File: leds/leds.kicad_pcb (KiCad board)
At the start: 4 copper layers, 68.8 x 135.2 mm, 96 parts, among them CN1 39302030, CN2 39288020, CN3 39288020, CN4 39288020, CN5 39302030, CN6 39288020, CN7 39288020, CN701 BM04B-SRSS-TB(LF)(SN), CN8 39288020, J202 Conn_01x06, J301 Conn_01x05_Pin, Q701 BSS138, Q702 BSS138, SW201 KEY-SMD_B3U-1000PM, SW202 KEY-SMD_B3U-1000PM, U1 SN74AHCT125PWR, U2 BTS70021EPPXUMA1, U201 ESP32-S3-WROOM-1, U3 BTS70021EPPXUMA1, U301 TPD6S300A, U302 TPS25730D, U401 TPS54202DDC, U402 CYA1040-15UH, U701 TPS73733DCQ_C5220270

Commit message: first draft
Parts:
- removed the CN5 at (-20.1, 157.0)
- removed LED201, LED202, LED203, LED204, LED205, LED206, LED207, LED208, LED209: WS2812B-2020, easyeda2kicad:LED-SMD_4P-L2.0-W2.0-TL_WS2812B-2020
- removed the U2 at (-35.5, 168.2)
- added CN10: 39302030, easyeda2kicad:CONN-TH_3P-P4.20_39302030, F.Cu at (105.6, 110.1)
- added CN11: 39288020, easyeda2kicad:CONN-TH_39288020, F.Cu at (105.9, 120.0)
- added CN12: 39288020, easyeda2kicad:CONN-TH_39288020, F.Cu at (105.9, 128.5)
- added CN13: 39288020, easyeda2kicad:CONN-TH_39288020, F.Cu at (105.9, 136.5)
- added CN14: 39302030, easyeda2kicad:CONN-TH_3P-P4.20_39302030, F.Cu at (140.6, 110.1)
- added CN15: 39288020, easyeda2kicad:CONN-TH_39288020, F.Cu at (140.9, 120.0)
- added CN16: 39288020, easyeda2kicad:CONN-TH_39288020, F.Cu at (140.9, 128.5)
- added CN17: 39288020, easyeda2kicad:CONN-TH_39288020, F.Cu at (140.9, 136.5)
- added CN9: 39288020, easyeda2kicad:CONN-TH_39288020, F.Cu at (70.9, 136.5)
- added FH10: 01550900M, easyeda2kicad:FUSE-SMD_L9.8-W5.0_01550900M, F.Cu at (91.4, 120.0)
- added FH11: 01550900M, easyeda2kicad:FUSE-SMD_L9.8-W5.0_01550900M, F.Cu at (91.4, 128.5)
- added FH12: 01550900M, easyeda2kicad:FUSE-SMD_L9.8-W5.0_01550900M, F.Cu at (91.4, 136.5)
- added FH13: 01550900M, easyeda2kicad:FUSE-SMD_L9.8-W5.0_01550900M, F.Cu at (126.4, 110.0)
- added FH14: 01550900M, easyeda2kicad:FUSE-SMD_L9.8-W5.0_01550900M, F.Cu at (126.4, 120.0)
- added FH15: 01550900M, easyeda2kicad:FUSE-SMD_L9.8-W5.0_01550900M, F.Cu at (126.4, 128.5)
- added FH16: 01550900M, easyeda2kicad:FUSE-SMD_L9.8-W5.0_01550900M, F.Cu at (126.4, 136.5)
- added FH9: 01550900M, easyeda2kicad:FUSE-SMD_L9.8-W5.0_01550900M, F.Cu at (91.4, 110.0)
- added H1: MountingHole_Pad, MountingHole:MountingHole_4mm_Pad_Via, F.Cu at (22.5, 81.0)
- added H2: MountingHole_Pad, MountingHole:MountingHole_4mm_Pad_Via, F.Cu at (139.5, 64.5)
- added H3: MountingHole_Pad, MountingHole:MountingHole_4mm_Pad_Via, F.Cu at (139.5, 81.0)
- added H4: MountingHole_Pad, MountingHole:MountingHole_4mm_Pad_Via, F.Cu at (22.5, 64.5)
- added H5: MountingHole_Pad, MountingHole:MountingHole_3.2mm_M3_Pad_Via, F.Cu at (16.0, 146.0)
- added H6: MountingHole_Pad, MountingHole:MountingHole_3.2mm_M3_Pad_Via, F.Cu at (146.0, 146.0)
- added H7: MountingHole_Pad, MountingHole:MountingHole_3.2mm_M3_Pad_Via, F.Cu at (16.0, 29.1)
- added H8: MountingHole_Pad, MountingHole:MountingHole_3.2mm_M3_Pad_Via, F.Cu at (146.0, 29.6)
- added R24: 820, Resistor_SMD:R_0603_1608Metric, F.Cu at (18.5, 92.0)
- added R25: 820, Resistor_SMD:R_0603_1608Metric, F.Cu at (53.5, 92.0)
- added R26: 820, Resistor_SMD:R_0603_1608Metric, F.Cu at (88.5, 92.0)
- added R27: 820, Resistor_SMD:R_0603_1608Metric, F.Cu at (123.5, 92.0)
- added TP10: LabeledTestPoint, easyeda2kicad:LabeledTestPoint, F.Cu at (89.0, 61.0)
- added TP11: LabeledTestPoint, easyeda2kicad:LabeledTestPoint, F.Cu at (99.5, 61.0)
- added TP12: LabeledTestPoint, easyeda2kicad:LabeledTestPoint, F.Cu at (110.0, 61.0)
- added TP13: LabeledTestPoint, easyeda2kicad:LabeledTestPoint, F.Cu at (75.0, 61.0)
- added TP14: LabeledTestPoint, easyeda2kicad:LabeledTestPoint, F.Cu at (85.5, 61.0)
- added TP15: LabeledTestPoint, easyeda2kicad:LabeledTestPoint, F.Cu at (96.0, 61.0)
- added TP16: LabeledTestPoint, easyeda2kicad:LabeledTestPoint, F.Cu at (106.5, 61.0)
- added TP5: LabeledTestPoint, easyeda2kicad:LabeledTestPoint, F.Cu at (82.0, 61.0)
- added TP6: LabeledTestPoint, easyeda2kicad:LabeledTestPoint, F.Cu at (92.5, 61.0)
- added TP7: LabeledTestPoint, easyeda2kicad:LabeledTestPoint, F.Cu at (103.0, 61.0)
- added TP8: LabeledTestPoint, easyeda2kicad:LabeledTestPoint, F.Cu at (113.5, 61.0)
- added TP9: LabeledTestPoint, easyeda2kicad:LabeledTestPoint, F.Cu at (78.4, 61.0)
- added U10: BTS70021EPPXUMA1, easyeda2kicad:PG-TSDSO-14_L4.9-W3.9-P0.65-LS6.0-BL-EP, F.Cu at (88.4, 98.0)
- added U11: BTS70021EPPXUMA1, easyeda2kicad:PG-TSDSO-14_L4.9-W3.9-P0.65-LS6.0-BL-EP, F.Cu at (123.4, 98.0)
- added U12: ADS1115IDGSR, easyeda2kicad:MSOP-10_L3.0-W3.0-P0.50-LS5.0-BL, F.Cu at (95.0, 50.0)
- added U9: BTS70021EPPXUMA1, easyeda2kicad:PG-TSDSO-14_L4.9-W3.9-P0.65-LS6.0-BL-EP, F.Cu at (53.4, 98.0)
- CN6: value 39288020 -> 39302030; footprint easyeda2kicad:CONN-TH_39288020 -> easyeda2kicad:CONN-TH_3P-P4.20_39302030
- moved CN6 100.8 mm to (70.6, 110.1), turned to 180 degrees
- moved FH5 95.3 mm to (56.4, 110.0)
- moved FH6 94.2 mm to (56.4, 120.0)
- moved FH7 93.5 mm to (56.4, 128.5)
- moved FH8 93.1 mm to (56.4, 136.5)
- moved CN7 91.8 mm to (70.9, 120.0), turned to 90 degrees
- moved CN8 83.4 mm to (70.9, 128.5), turned to 90 degrees
- moved SW1 82.4 mm to (123.3, 32.8)
- moved U1 80.7 mm to (114.0, 49.5), turned to -90 degrees
- moved SW2 69.7 mm to (128.8, 32.8)
- moved R22 64.9 mm to (141.7, 50.5)
- moved CN1 64.9 mm to (146.8, 48.0)
- moved Q1 64.9 mm to (141.3, 53.0)
- moved Q2 64.9 mm to (141.3, 46.0)
- moved R21 64.9 mm to (141.8, 48.8)
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- renumbered C204 to C1, C306 to C10, C307 to C11, C308 to C12, C309 to C13, C310 to C14, C311 to C15, C312 to C16, C313 to C17, C401 to C18, C402 to C19, C201 to C2, C403 to C20, C404 to C21, C405 to C22, C406 to C23, C701 to C24, C702 to C25, C703 to C26, C704 to C27, C202 to C3, C203 to C4, C301 to C5, C302 to C6, C303 to C7, C304 to C8, C305 to C9, CN701 to CN1, CN1 to CN2, CN2 to CN3, CN3 to CN4, CN4 to CN5, J202 to J1, J301 to J2, Q701 to Q1, Q702 to Q2, R202 to R1, R306 to R10, R307 to R11, R308 to R12, R309 to R13, R310 to R14, R311 to R15, R312 to R16, R313 to R17, R401 to R18, R402 to R19, R203 to R2, R403 to R20, R702 to R21, R703 to R22, R701 to R23, R204 to R3, R201 to R4, R301 to R5, R302 to R6, R303 to R7, R304 to R8, R305 to R9, SW202 to SW1, SW201 to SW2, TP301 to TP1, TP302 to TP2, TP303 to TP3, TP401 to TP4, U201 to U2, U301 to U3, U302 to U4, U401 to U5, U402 to U6, U701 to U7, U3 to U8, USBC301 to USBC1
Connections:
- net /esp32/I2C.SCL renamed /a2d/I2C.SCL
- net /esp32/I2C.SDA renamed /a2d/I2C.SDA
- CN2 pad 1: (no net) -> Net-(CN2-Pad1)
- CN2 pad 2: /led_channel/DIN -> /esp32/LED1
- CN3 pad 1: unconnected-(FH2-Pad2) -> Net-(CN3-Pad1)
- CN6 pad 2: GND -> /esp32/LED2
- FH1 pad 2: (no net) -> Net-(CN2-Pad1)
- FH2 pad 2: unconnected-(FH2-Pad2) -> Net-(CN3-Pad1)
- FH5 pad 2: Net-(CN5-Pad1) (its old number) -> Net-(CN6-Pad1)
- FH6 pad 2: Net-(CN6-Pad1) -> Net-(CN7-Pad1)
- FH7 pad 2: Net-(CN7-Pad1) -> Net-(CN8-Pad1)
- FH8 pad 2: Net-(CN8-Pad1) -> Net-(CN9-Pad1)
- U1 pad 1: unconnected-(U1-~{1OE}-Pad1) -> GND
- U1 pad 10: unconnected-(U1-~{3OE}-Pad10) -> GND
- U1 pad 11: unconnected-(U1-4Y-Pad11) -> /esp32/LED3
- U1 pad 12: unconnected-(U1-4A-Pad12) -> Net-(U1-4A)
- U1 pad 13: unconnected-(U1-~{4OE}-Pad13) -> GND
- U1 pad 2: unconnected-(U1-1A-Pad2) -> Net-(U1-1A)
- U1 pad 3: unconnected-(U1-1Y-Pad3) -> /esp32/LED2
- U1 pad 4: unconnected-(U1-~{2OE}-Pad4) -> GND
- U1 pad 5: unconnected-(U1-2A-Pad5) -> Net-(U1-2A)
- U1 pad 6: unconnected-(U1-2Y-Pad6) -> /esp32/LED1
- U1 pad 7: unconnected-(U1-GND-Pad7) -> GND
- U1 pad 8: unconnected-(U1-3Y-Pad8) -> /esp32/LED4
- U1 pad 9: unconnected-(U1-3A-Pad9) -> Net-(U1-3A)
- U2 pad 10: unconnected-(U201-IO17-Pad10) -> /esp32/EN3
- U2 pad 11: unconnected-(U201-IO18-Pad11) -> /esp32/EN4
- U2 pad 19: unconnected-(U201-IO11-Pad19) -> Net-(U1-2A)
- U2 pad 20: unconnected-(U201-IO12-Pad20) -> Net-(U1-1A)
- U2 pad 21: unconnected-(U201-IO13-Pad21) -> Net-(U1-4A)
- U2 pad 22: unconnected-(U201-IO14-Pad22) -> Net-(U1-3A)
- U2 pad 31: Net-(LED201-DI) -> unconnected-(U2-IO38-Pad31)
- U2 pad 8: unconnected-(U201-IO15-Pad8) -> /esp32/EN1
- U2 pad 9: unconnected-(U201-IO16-Pad9) -> /esp32/EN2
- U8 pad 11: (no net) -> unconnected-(U8-n.c.-Pad11)
- U8 pad 15: /led_channel/12V -> /buckconverter/VIN
- U8 pad 2: /led_channel/IN -> /esp32/EN1
- U8 pad 4: /led_channel/IS -> /a2d/AIN1
- U8 pad 5: (no net) -> unconnected-(U8-n.c.-Pad5)
- U8 pad 6: (no net) -> unconnected-(U8-n.c.-Pad6)
- U8 pad 7: (no net) -> unconnected-(U8-n.c.-Pad7)
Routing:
- net /esp32/LED1: track 0.00 -> 112.0 mm, vias 0 -> 1
- net /esp32/EN1: track 0.00 -> 109.6 mm, vias 0 -> 2
- net /a2d/AIN1: track 0.00 -> 94.9 mm, vias 0 -> 1
- net /esp32/LED2: track 0.00 -> 88.6 mm, vias 0 -> 1
- net /esp32/EN2: track 0.00 -> 79.8 mm, vias 0 -> 2
- net /esp32/LED4: track 0.00 -> 72.5 mm, vias 0 -> 1
- net /esp32/EN4: track 0.00 -> 72.1 mm, vias 0 -> 2
- net /5V: track 51.8 -> 123.2 mm, vias 15 -> 5
- net /esp32/LED3: track 0.00 -> 68.7 mm, vias 0 -> 1
- net /esp32/EN3: track 0.00 -> 67.4 mm, vias 0 -> 2
- net /a2d/AIN2: track 0.00 -> 61.8 mm, vias 0 -> 1
- net /a2d/AIN4: track 0.00 -> 57.2 mm, vias 0 -> 1
- net /esp32/USB.DN: track 38.0 -> 90.7 mm
- net /esp32/USB.DP: track 37.4 -> 87.0 mm
- net /a2d/AIN3: track 0.00 -> 49.0 mm, vias 0 -> 1
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- added copper zone on F.Cu, net /led_channel/Switched12V
- added copper zone on F.Cu, net /led_channel1/Switched12V
- added copper zone on F.Cu, net /led_channel2/Switched12V
- added copper zone on F.Cu, net /led_channel3/Switched12V
- added copper zone on F.Cu, net GND
- added copper zone on In2.Cu, net GND
- removed copper zone on F.Cu, net /led_channel/12V
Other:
- board size 68.8 x 135.2 mm -> 138 x 125 mm
- board text added: "LEDs v0.1"
- board text removed: "espamp v0.2"

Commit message: First revision of LEDs sent to fab
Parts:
- added C28: 100nF, Capacitor_SMD:C_0603_1608Metric, F.Cu at (99.5, 51.0)
- added C29: 1uF, Capacitor_SMD:C_0603_1608Metric, F.Cu at (101.0, 51.0)
- R11: value 9.31k -> 162k
- R12: value 191k -> 38.3k
- R8: value 37.4 -> 38.3k
- moved H1 16.5 mm to (22.5, 64.5)
- moved H4 16.5 mm to (22.5, 81.0)
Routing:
- net GND: track 65.4 -> 66.9 mm, vias 47 -> 49
- net /a2d/AIN4: track 57.2 -> 58.3 mm
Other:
- board text added: "LED1"
- board text added: "LED2"
- board text added: "LED3"
- board text added: "LED4"
- board text added: "V+"

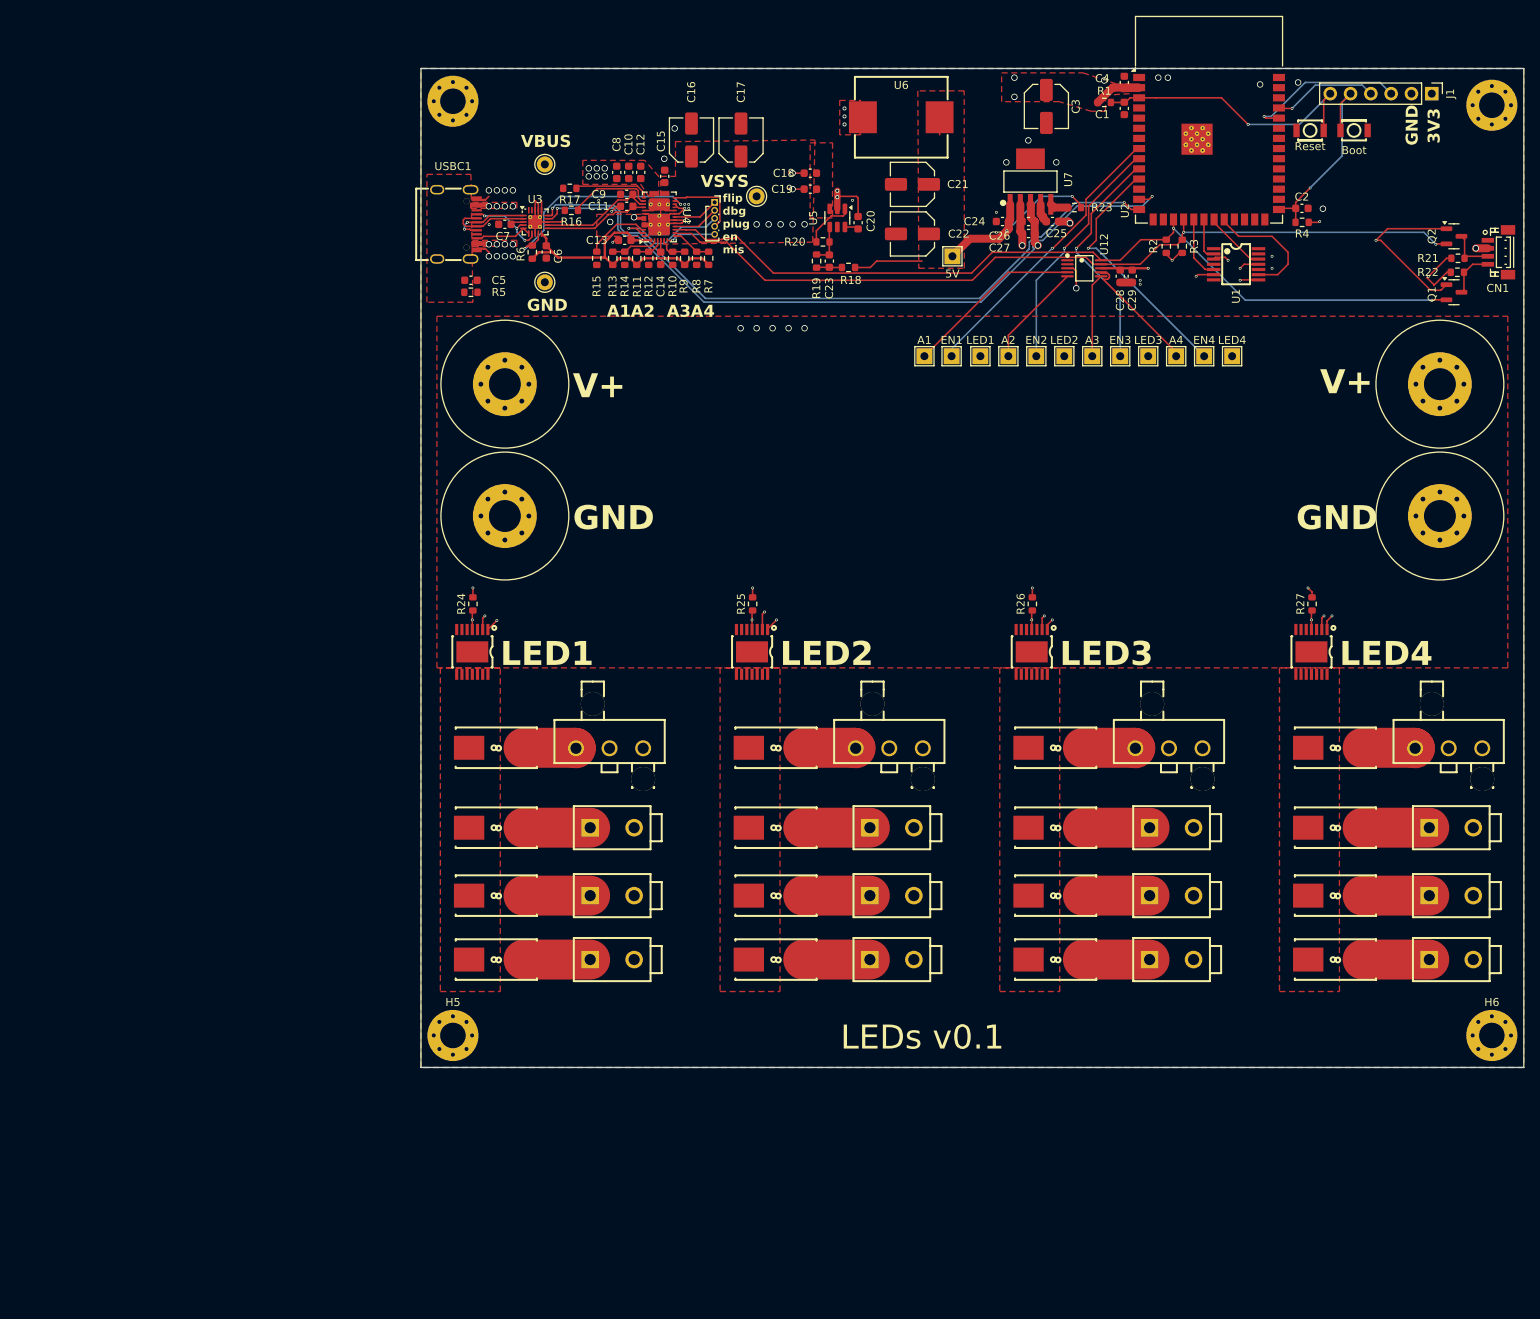
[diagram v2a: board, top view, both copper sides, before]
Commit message: Fix errors in LEDs. Revision 0.2 ready to fab.
- [x] Connect VCC on level shifter
- [x] Connect DEN with pull-up
- [x] Add channel on indicator LED - 3.3k
- [x] Flip 3 pin connector
- [x] 82 ohm damping resistor on LED drivers
- [x] Add status LED - white 220 - sinking to ESP
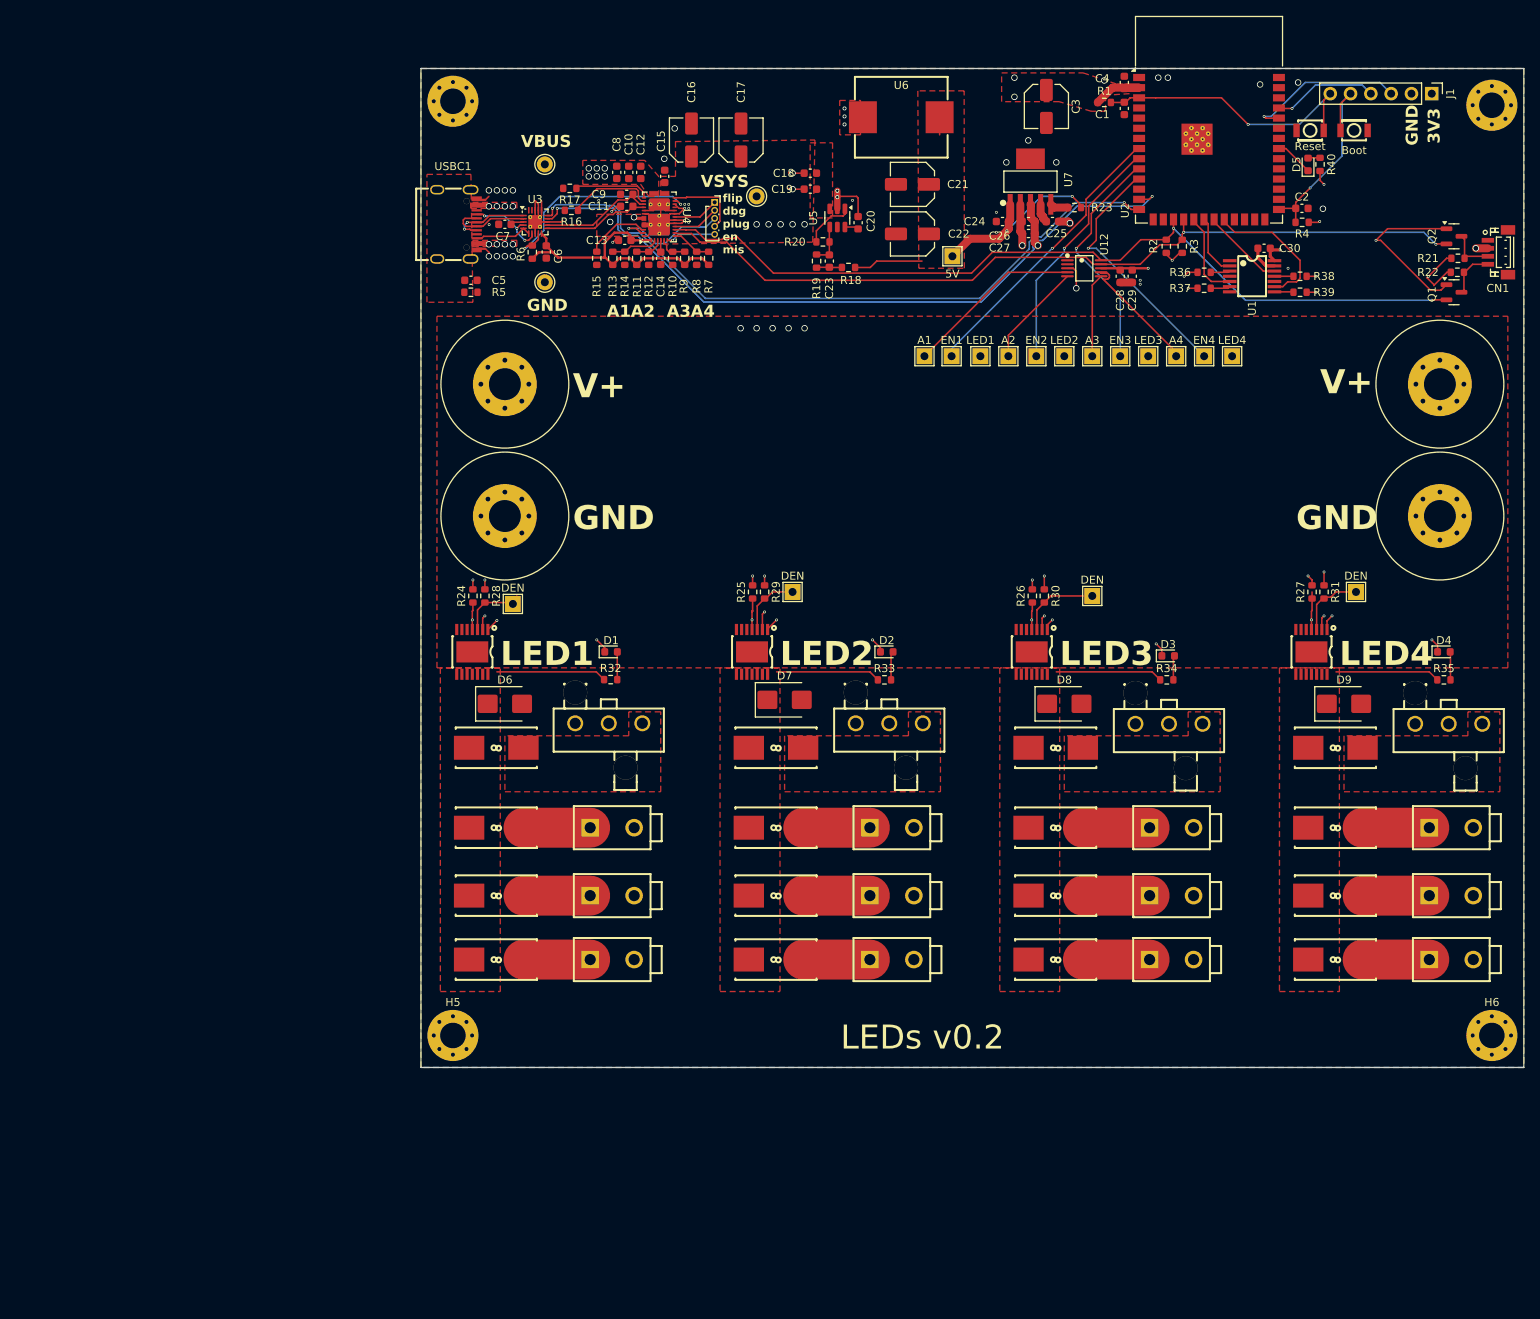
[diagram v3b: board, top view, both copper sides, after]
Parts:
- added C30: 100nF, Capacitor_SMD:C_0603_1608Metric, F.Cu at (117.5, 47.5)
- added D1: LED, LED_SMD:LED_0603_1608Metric, F.Cu at (35.8, 98.0)
- added D2: LED, LED_SMD:LED_0603_1608Metric, F.Cu at (70.3, 98.0)
- added D3: LED, LED_SMD:LED_0603_1608Metric, F.Cu at (105.5, 98.5)
- added D4: LED, LED_SMD:LED_0603_1608Metric, F.Cu at (140.0, 98.0)
- added D5: LED, LED_SMD:LED_0603_1608Metric, F.Cu at (123.0, 37.0)
- added D6: D_TVS, Diode_SMD:D_SMB, F.Cu at (22.5, 104.5)
- added D7: D_TVS, Diode_SMD:D_SMB, F.Cu at (57.5, 104.0)
- added D8: D_TVS, Diode_SMD:D_SMB, F.Cu at (92.5, 104.5)
- added D9: D_TVS, Diode_SMD:D_SMB, F.Cu at (127.5, 104.5)
- added R28: 4.7k, Resistor_SMD:R_0603_1608Metric, F.Cu at (20.0, 91.0)
- added R29: 4.7k, Resistor_SMD:R_0603_1608Metric, F.Cu at (55.0, 90.5)
- added R30: 4.7k, Resistor_SMD:R_0603_1608Metric, F.Cu at (90.0, 91.0)
- added R31: 4.7k, Resistor_SMD:R_0603_1608Metric, F.Cu at (125.0, 90.5)
- added R32: 3.3k, Resistor_SMD:R_0603_1608Metric, F.Cu at (35.7, 101.5)
- added R33: 3.3k, Resistor_SMD:R_0603_1608Metric, F.Cu at (70.0, 101.5)
- added R34: 3.3k, Resistor_SMD:R_0603_1608Metric, F.Cu at (105.3, 101.5)
- added R35: 3.3k, Resistor_SMD:R_0603_1608Metric, F.Cu at (140.0, 101.5)
- added R36: 82, Resistor_SMD:R_0603_1608Metric, F.Cu at (110.0, 50.5)
- added R37: 82, Resistor_SMD:R_0603_1608Metric, F.Cu at (110.0, 52.5)
- added R38: 82, Resistor_SMD:R_0603_1608Metric, F.Cu at (122.0, 51.0)
- added R39: 82, Resistor_SMD:R_0603_1608Metric, F.Cu at (122.0, 53.0)
- added R40: 330, Resistor_SMD:R_0603_1608Metric, F.Cu at (124.5, 37.0)
- added TP17: LabeledTestPoint, easyeda2kicad:LabeledTestPoint, F.Cu at (23.5, 92.0)
- added TP18: LabeledTestPoint, easyeda2kicad:LabeledTestPoint, F.Cu at (58.5, 90.5)
- added TP19: LabeledTestPoint, easyeda2kicad:LabeledTestPoint, F.Cu at (96.0, 91.0)
- added TP20: LabeledTestPoint, easyeda2kicad:LabeledTestPoint, F.Cu at (129.0, 90.5)
- R24, R25, R26, R27: value 820 -> 1.5k
- moved CN2 3.13 mm to (35.5, 106.9), turned to 0 degrees
- moved CN6 3.12 mm to (70.6, 106.9), turned to 0 degrees
- moved CN10 3.06 mm to (105.6, 107.0), turned to 0 degrees
- moved CN14 3.06 mm to (140.6, 107.0), turned to 0 degrees
- moved U1 2.50 mm to (116.0, 51.0)
- moved R25 1.50 mm to (53.5, 90.5)
- moved R27 1.50 mm to (123.5, 90.5)
- moved R24 1.00 mm to (18.5, 91.0)
- moved R26 1.00 mm to (88.5, 91.0)
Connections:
- net Net-(CN10-Pad1) renamed /led_channel2/Fused1
- net Net-(CN14-Pad1) renamed /led_channel3/Fused1
- net Net-(CN2-Pad1) renamed /led_channel/Fused1
- net Net-(CN6-Pad1) renamed /led_channel1/Fused1
- U1 pad 11: /esp32/LED3 -> Net-(U1-4Y)
- U1 pad 14: unconnected-(U1-VCC-Pad14) -> /5V
- U1 pad 3: /esp32/LED2 -> Net-(U1-1Y)
- U1 pad 6: /esp32/LED1 -> Net-(U1-2Y)
- U1 pad 8: /esp32/LED4 -> Net-(U1-3Y)
- U10 pad 3: /led_channel2/DEN -> Net-(U10-DEN)
- U11 pad 3: /led_channel3/DEN -> Net-(U11-DEN)
- U2 pad 33: unconnected-(U2-IO40-Pad33) -> Net-(D5-K)
- U8 pad 3: /led_channel/DEN -> Net-(U8-DEN)
- U9 pad 3: /led_channel1/DEN -> Net-(U9-DEN)
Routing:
- net /led_channel/Switched12V: track 0.00 -> 13.8 mm
- net /led_channel2/Switched12V: track 0.00 -> 13.4 mm
- net /led_channel3/Switched12V: track 0.00 -> 13.1 mm
- net /led_channel1/Switched12V: track 0.00 -> 13.1 mm
- net GND: track 66.9 -> 78.0 mm, vias 49 -> 52
- net Net-(U10-DEN): track 0.00 -> 10.1 mm
- net Net-(U11-DEN): track 0.00 -> 8.70 mm
- net /5V: track 123.2 -> 131.8 mm, vias 5 -> 10
- net Net-(U8-DEN): track 0.00 -> 8.10 mm
- net /esp32/LED2: track 88.6 -> 80.5 mm
- net Net-(U9-DEN): track 0.00 -> 7.10 mm
- net /led_channel3/Fused1: track 6.60 -> 0.00 mm
- net /led_channel2/Fused1: track 6.60 -> 0.00 mm
- net /led_channel1/Fused1: track 6.60 -> 0.00 mm
- net /led_channel/Fused1: track 6.60 -> 0.00 mm
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- added copper zone on F.Cu, net /led_channel/Fused1
- added copper zone on F.Cu, net /led_channel1/Fused1
- added copper zone on F.Cu, net /led_channel2/Fused1
- added copper zone on F.Cu, net /led_channel3/Fused1
- removed copper zone on In2.Cu, net GND
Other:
- board text added: "LEDs v0.2"
- board text removed: "LEDs v0.1"
